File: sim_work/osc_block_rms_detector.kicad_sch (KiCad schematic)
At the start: 3 parts

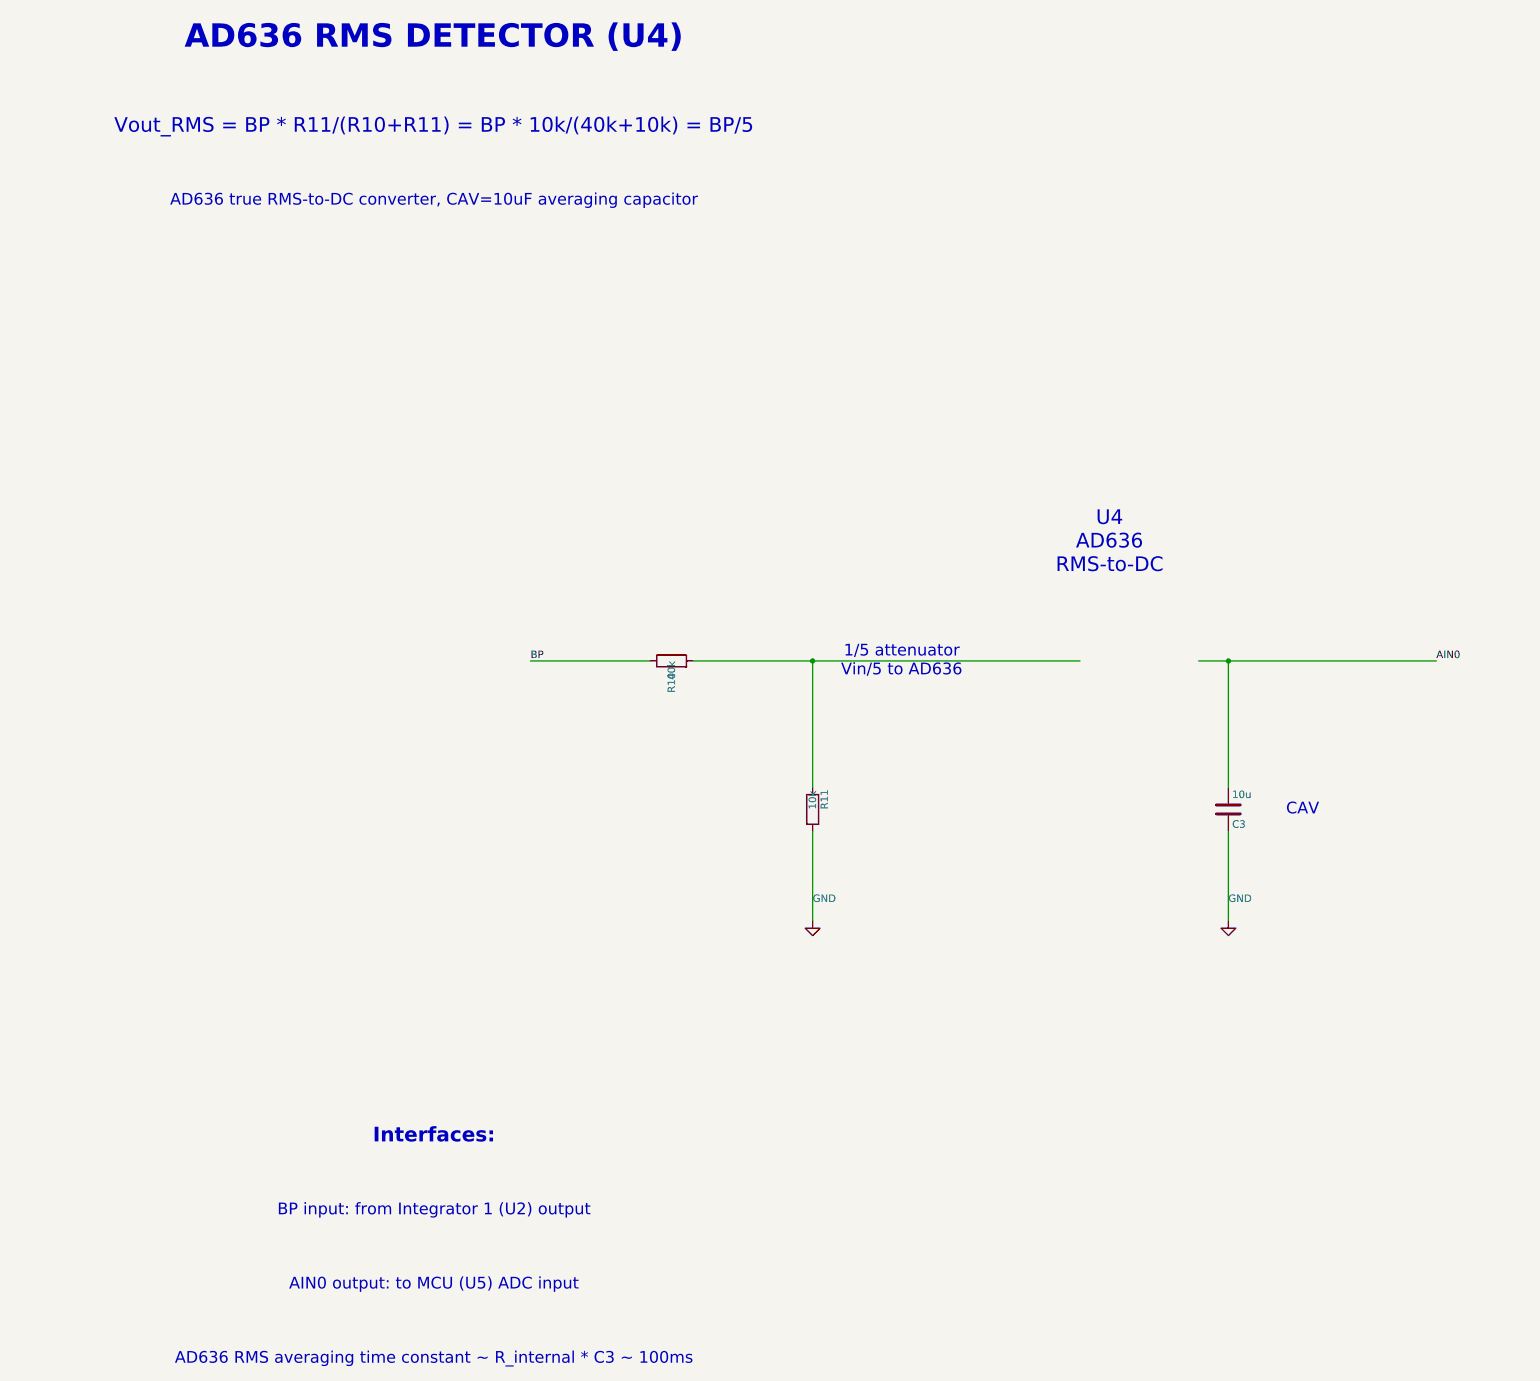
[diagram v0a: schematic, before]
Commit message: Fix schematic connections, add docs and repo portability
- Input filters: R rotation=90 (horizontal), ESD diode rotations fixed,
  junction dots at cathode-signal connection, wires to GND symbols
- Relay ladder: flyback diode rotation 270->90 (K top, A bottom)
- Electrometer/Mux TIA: 4 junction dots each at T-junctions
- AD636 RMS detector: proper IC box with pin labels replaces text-only
- Oscillator blocks: D_Zener symbol, L-shaped cathode routing
- TIA blocks: title/function annotations on all 5 blocks
- New: requirements.txt, docs/oscillator_guide.md
- D_Zener.kicad_sym added to bundled symbols/
- .gitignore updated for docs/ and requirements.txt
- README updated with pip install -r requirements.txt
- PROJECT.md session 9 changelog
- SimGUI builds clean (0 errors)

Co-Authored-By: Claude Opus 4.6 <noreply@anthropic.com>
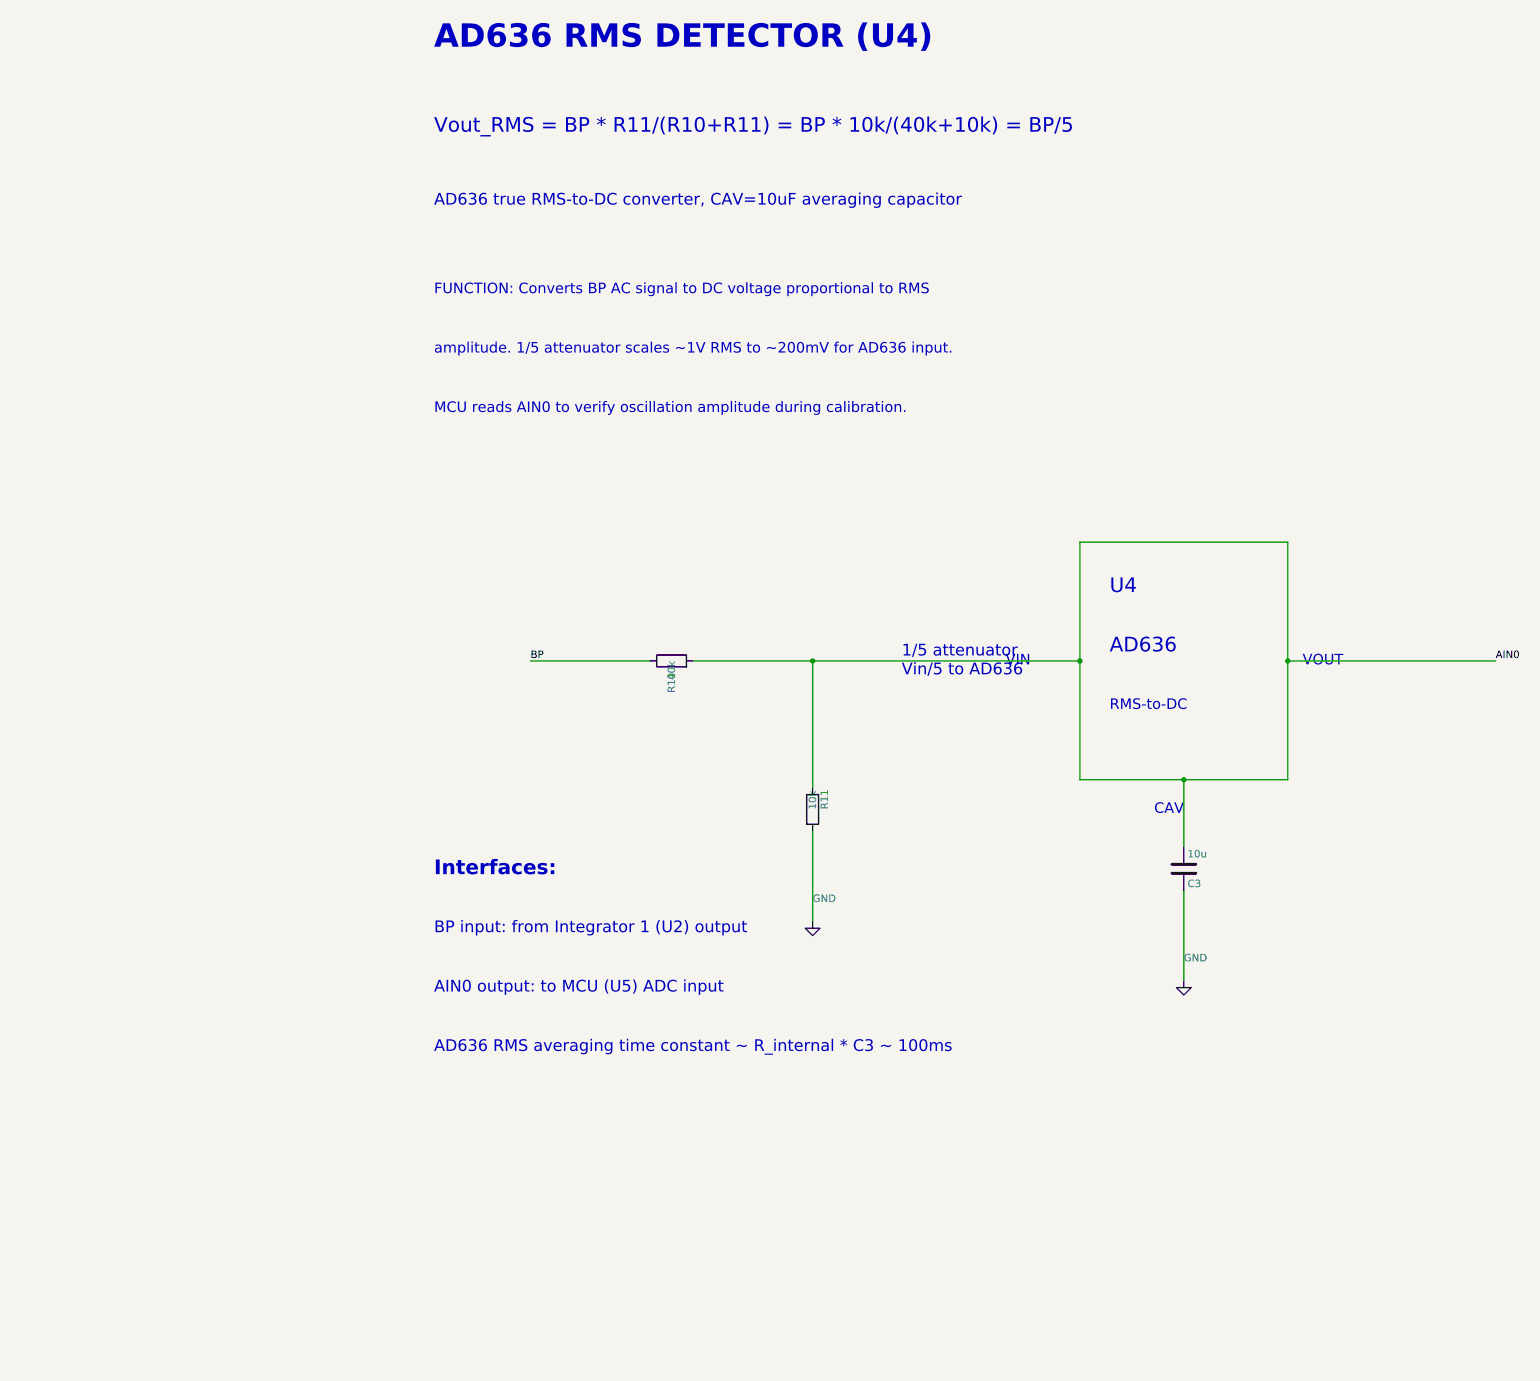
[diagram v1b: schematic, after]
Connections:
- net AIN0: now also R10.2, R11.1
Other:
- note added: "AD636"
- note added: "FUNCTION: Converts BP AC signal to DC voltage proportional to RMS"
- note added: "MCU reads AIN0 to verify oscillation amplitude during calibration."
- note added: "RMS-to-DC"
- note added: "U4"
- note added: "VIN"
- note added: "VOUT"
- note added: "amplitude. 1/5 attenuator scales ~1V RMS to ~200mV for AD636 input."
- note removed: "U4 AD636 RMS-to-DC"
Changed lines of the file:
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@@
 		(instances
 			(project "Oscillator - RMS Detector"
-				(path "/6abdfe07-2f4a-4a79-89a5-9ae6e7ff0a79"
+				(path "/042bf1bb-c13b-45a5-b8e4-6eb55b7897a6"
 					(reference "R10")
 					(unit 1)
@@
 		(instances
 			(project "Oscillator - RMS Detector"
-				(path "/6abdfe07-2f4a-4a79-89a5-9ae6e7ff0a79"
+				(path "/042bf1bb-c13b-45a5-b8e4-6eb55b7897a6"
 					(reference "R11")
 					(unit 1)
@@
 		(instances
 			(project "Oscillator - RMS Detector"
-				(path "/6abdfe07-2f4a-4a79-89a5-9ae6e7ff0a79"
+				(path "/042bf1bb-c13b-45a5-b8e4-6eb55b7897a6"
 					(reference "#PWR001")
 					(unit 1)
@@
 	(symbol
 		(lib_id "C:C")
-		(at 156.21 147.32 0)
+		(at 148.59 157.48 0)
 		(unit 1)
 		(exclude_from_sim no)
@@
 		(fields_autoplaced no)
 		(property "Reference" "C3"
-			(at 156.845 149.86 0.0000)
+			(at 149.225 160.02 0.0000)
 			(effects
 				(font
@@
 		)
 		(property "Value" "10u"
-			(at 156.845 144.78 0.0000)
+			(at 149.225 154.94 0.0000)
 			(effects
 				(font
@@
 		(instances
 			(project "Oscillator - RMS Detector"
-				(path "/6abdfe07-2f4a-4a79-89a5-9ae6e7ff0a79"
+				(path "/042bf1bb-c13b-45a5-b8e4-6eb55b7897a6"
 					(reference "C3")
 					(unit 1)
@@
 	(symbol
 		(lib_id "GND:GND")
-		(at 156.21 166.37 0)
+		(at 148.59 176.53 0)
 		(unit 1)
 		(exclude_from_sim no)
@@
 		(fields_autoplaced no)
 		(property "Reference" "#PWR002"
-			(at 156.21 160.02 0.0000)
+			(at 148.59 170.18 0.0000)
 			(hide yes)
 			(effects
@@
 		)
 		(property "Value" "GND"
-			(at 156.21 162.56 0.0000)
+			(at 148.59 172.72 0.0000)
 			(effects
 				(font
@@
 		(instances
 			(project "Oscillator - RMS Detector"
-				(path "/6abdfe07-2f4a-4a79-89a5-9ae6e7ff0a79"
+				(path "/042bf1bb-c13b-45a5-b8e4-6eb55b7897a6"
 					(reference "#PWR002")
 					(unit 1)
@@
 	(wire
 		(pts
-			(xy 151.13 121.92) (xy 156.21 121.92)
-		)
-		(stroke
-			(width 0)
-			(type default)
-		)
-	)
-	(wire
-		(pts
-			(xy 156.21 121.92) (xy 156.21 143.51)
-		)
-		(stroke
-			(width 0)
-			(type default)
-		)
-	)
-	(wire
-		(pts
-			(xy 156.21 151.13) (xy 156.21 166.37)
-		)
-		(stroke
-			(width 0)
-			(type default)
-		)
-	)
-	(wire
-		(pts
-			(xy 156.21 121.92) (xy 191.77 121.92)
+			(xy 130.81 101.6) (xy 166.37 101.6)
+		)
+		(stroke
+			(width 0)
+			(type default)
+		)
+	)
+	(wire
+		(pts
+			(xy 166.37 101.6) (xy 166.37 142.24)
+		)
+		(stroke
+			(width 0)
+			(type default)
+		)
+	)
+	(wire
+		(pts
+			(xy 166.37 142.24) (xy 130.81 142.24)
+		)
+		(stroke
+			(width 0)
+			(type default)
+		)
+	)
+	(wire
+		(pts
+			(xy 130.81 142.24) (xy 130.81 101.6)
+		)
+		(stroke
+			(width 0)
+			(type default)
+		)
+	)
+	(wire
+		(pts
+			(xy 148.59 142.24) (xy 148.59 153.67)
+		)
+		(stroke
+			(width 0)
+			(type default)
+		)
+	)
+	(wire
+		(pts
+			(xy 148.59 161.29) (xy 148.59 176.53)
+		)
+		(stroke
+			(width 0)
+			(type default)
+		)
+	)
+	(wire
+		(pts
+			(xy 166.37 121.92) (xy 201.93 121.92)
 		)
 		(stroke
@@
 	)
 	(junction
-		(at 156.21 121.92)
+		(at 130.81 121.92)
 		(diameter 0)
 		(color 0 0 0 0)
 	)
+	(junction
+		(at 148.59 142.24)
+		(diameter 0)
+		(color 0 0 0 0)
+	)
+	(junction
+		(at 166.37 121.92)
+		(diameter 0)
+		(color 0 0 0 0)
+	)
 	(label "BP"
 		(at 36.83 121.92 0)
@@
 	)
 	(label "AIN0"
-		(at 191.77 121.92 0)
+		(at 201.93 121.92 0)
 		(effects
 			(font
@@
 				(bold yes)
 			)
+			(justify left)
 		)
 	)
@@
 				(size 2.5 2.5)
 			)
+			(justify left)
 		)
 	)
@@
 				(size 2 2)
 			)
+			(justify left)
+		)
+	)
+	(text "FUNCTION: Converts BP AC signal to DC voltage proportional to RMS"
+		(exclude_from_sim no)
+		(at 20.32 58.42 0.0000)
+		(effects
+			(font
+				(size 1.8 1.8)
+			)
+			(justify left)
+		)
+	)
+	(text "amplitude. 1/5 attenuator scales ~1V RMS to ~200mV for AD636 input."
+		(exclude_from_sim no)
+		(at 20.32 68.58 0.0000)
+		(effects
+			(font
+				(size 1.8 1.8)
+			)
+			(justify left)
+		)
+	)
+	(text "MCU reads AIN0 to verify oscillation amplitude during calibration."
+		(exclude_from_sim no)
+		(at 20.32 78.74 0.0000)
+		(effects
+			(font
+				(size 1.8 1.8)
+			)
+			(justify left)
 		)
 	)
@@
 				(size 2 2)
 			)
-		)
-	)
-	(text "U4\nAD636\nRMS-to-DC"
-		(exclude_from_sim no)
-		(at 135.89 101.6 0.0000)
+			(justify left)
+		)
+	)
+	(text "U4"
+		(exclude_from_sim no)
+		(at 135.89 109.22 0.0000)
 		(effects
 			(font
 				(size 2.5 2.5)
 			)
+			(justify left)
+		)
+	)
+	(text "AD636"
+		(exclude_from_sim no)
+		(at 135.89 119.38 0.0000)
+		(effects
+			(font
+				(size 2.5 2.5)
+			)
+			(justify left)
+		)
+	)
+	(text "RMS-to-DC"
+		(exclude_from_sim no)
+		(at 135.89 129.54 0.0000)
+		(effects
+			(font
+				(size 1.8 1.8)
+			)
+			(justify left)
+		)
+	)
+	(text "VIN"
+		(exclude_from_sim no)
+		(at 118.11 121.92 0.0000)
+		(effects
+			(font
+				(size 1.8 1.8)
+			)
+			(justify left)
+		)
+	)
+	(text "VOUT"
+		(exclude_from_sim no)
+		(at 168.91 121.92 0.0000)
+		(effects
+			(font
+				(size 1.8 1.8)
+			)
+			(justify left)
 		)
 	)
 	(text "CAV"
 		(exclude_from_sim no)
-		(at 168.91 147.32 0.0000)
-		(effects
-			(font
-				(size 2 2)
-			)
+		(at 143.51 147.32 0.0000)
+		(effects
+			(font
+				(size 1.8 1.8)
+			)
+			(justify left)
 		)
 	)
 	(text "Interfaces:"
 		(exclude_from_sim no)
-		(at 20.32 203.2 0.0000)
+		(at 20.32 157.48 0.0000)
 		(effects
 			(font
@@
 				(bold yes)
 			)
+			(justify left)
 		)
 	)
 	(text "BP input: from Integrator 1 (U2) output"
 		(exclude_from_sim no)
-		(at 20.32 215.9 0.0000)
+		(at 20.32 167.64 0.0000)
 		(effects
 			(font
 				(size 2 2)
 			)
+			(justify left)
 		)
 	)
 	(text "AIN0 output: to MCU (U5) ADC input"
 		(exclude_from_sim no)
-		(at 20.32 228.6 0.0000)
+		(at 20.32 177.8 0.0000)
 		(effects
 			(font
 				(size 2 2)
 			)
+			(justify left)
 		)
 	)
 	(text "AD636 RMS averaging time constant ~ R_internal * C3 ~ 100ms"
 		(exclude_from_sim no)
-		(at 20.32 241.3 0.0000)
+		(at 20.32 187.96 0.0000)
 		(effects
 			(font
 				(size 2 2)
 			)
-		)
-	)
+			(justify left)
+		)
+	)
